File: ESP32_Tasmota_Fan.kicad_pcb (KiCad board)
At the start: 2 copper layers, 70 x 45 mm, 19 parts, among them J1 Conn_01x04, J2 Conn_01x06, J6 Conn_01x02_Female, J8 Conn_01x06, U1 mini_esp32

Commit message: Production Version
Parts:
- H1, H2, H3, H4: footprint MountingHole:MountingHole_3.2mm_M3_ISO7380 -> MountingHole:MountingHole_3.2mm_M3_Pad_Via
- moved J6 1.42 mm to (144.8, 133.5)
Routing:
- net Net-(D1-Pad2): track 0.00 -> 2.90 mm
- net +12V: track 99.6 -> 101.1 mm

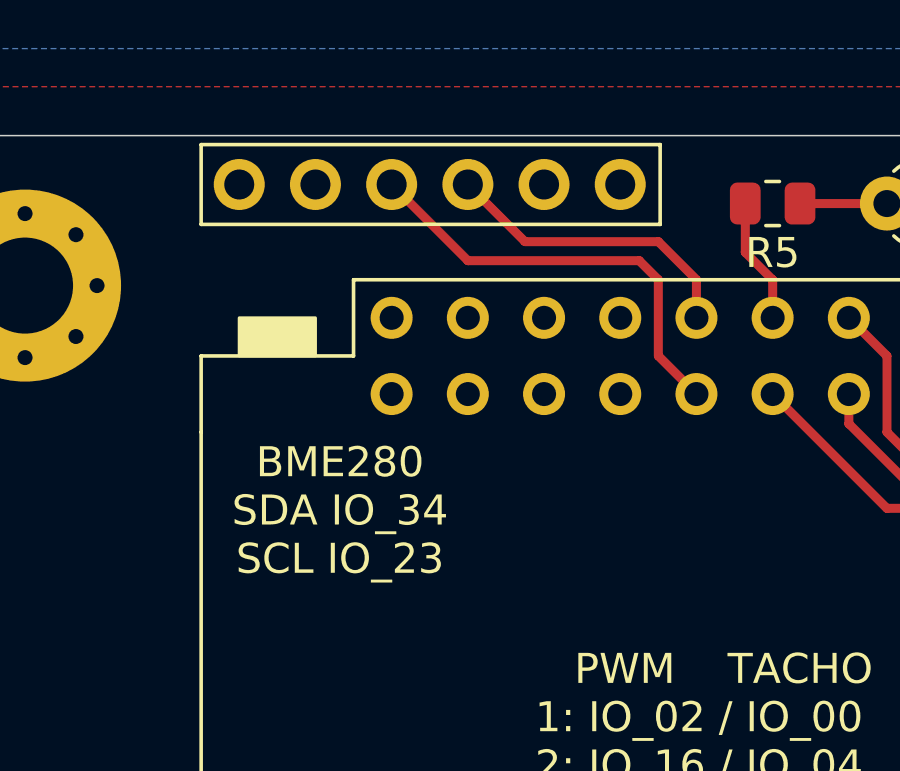
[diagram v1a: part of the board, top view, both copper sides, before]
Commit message: Move I2C Pins for BME280
IO34 can only do input, so it is not suitable for I2C
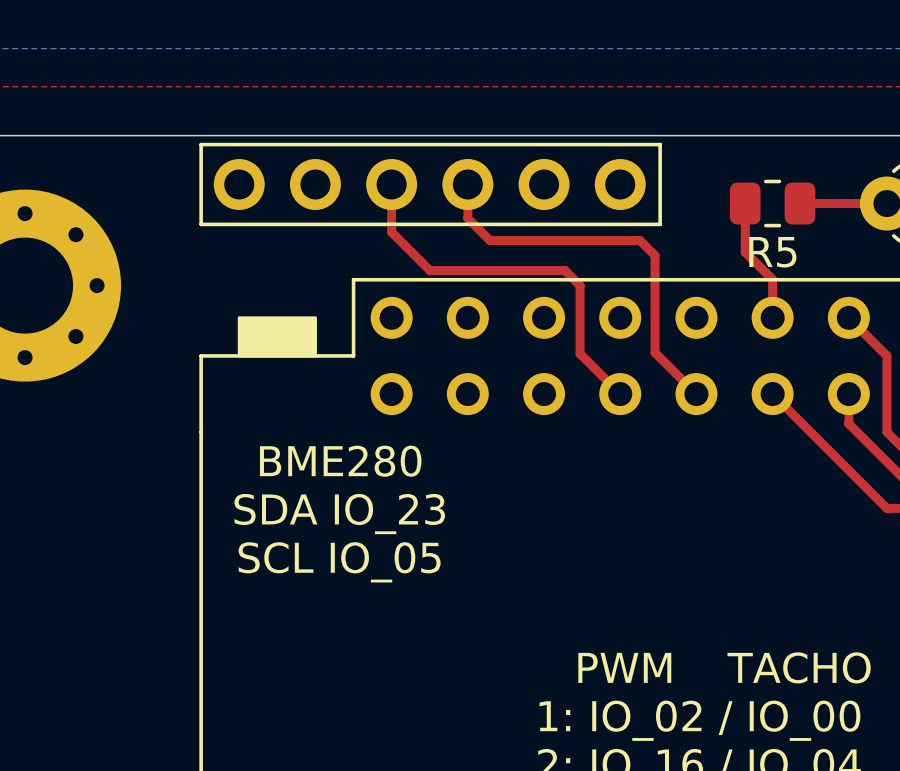
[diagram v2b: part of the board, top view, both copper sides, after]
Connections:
- U1 pad 11: SDA -> Net-(U1-Pad11)
- U1 pad 12: SCL -> SDA
- U1 pad 14: Net-(U1-Pad14) -> SCL
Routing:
- net SDA: track 10.2 -> 13.1 mm
- net SCL: track 14.5 -> 12.8 mm
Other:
- board text added: "BME280 SDA IO_23 SCL IO_05"
- board text removed: "BME280 SDA IO_34 SCL IO_23"

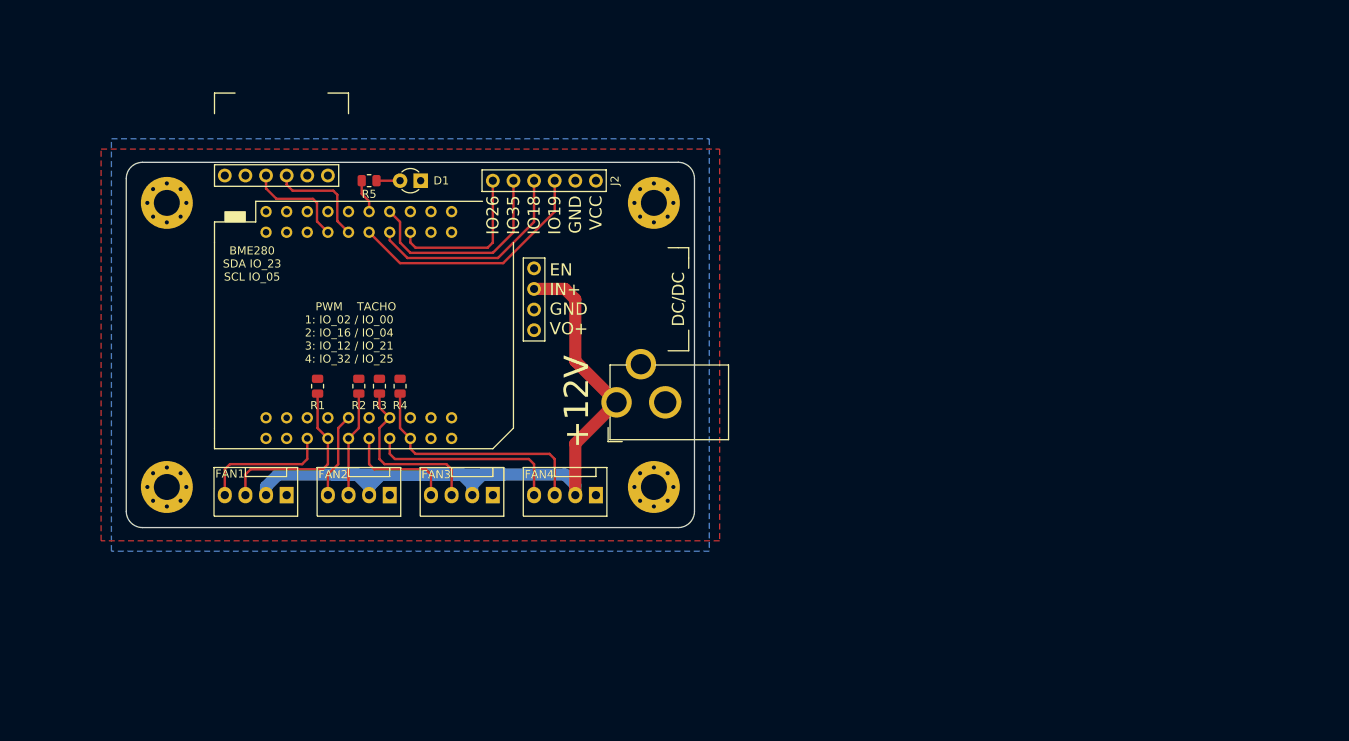
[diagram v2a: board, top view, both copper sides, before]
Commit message: First step for new design
split up design into multiples
added voltage regulator available at JLCPCB
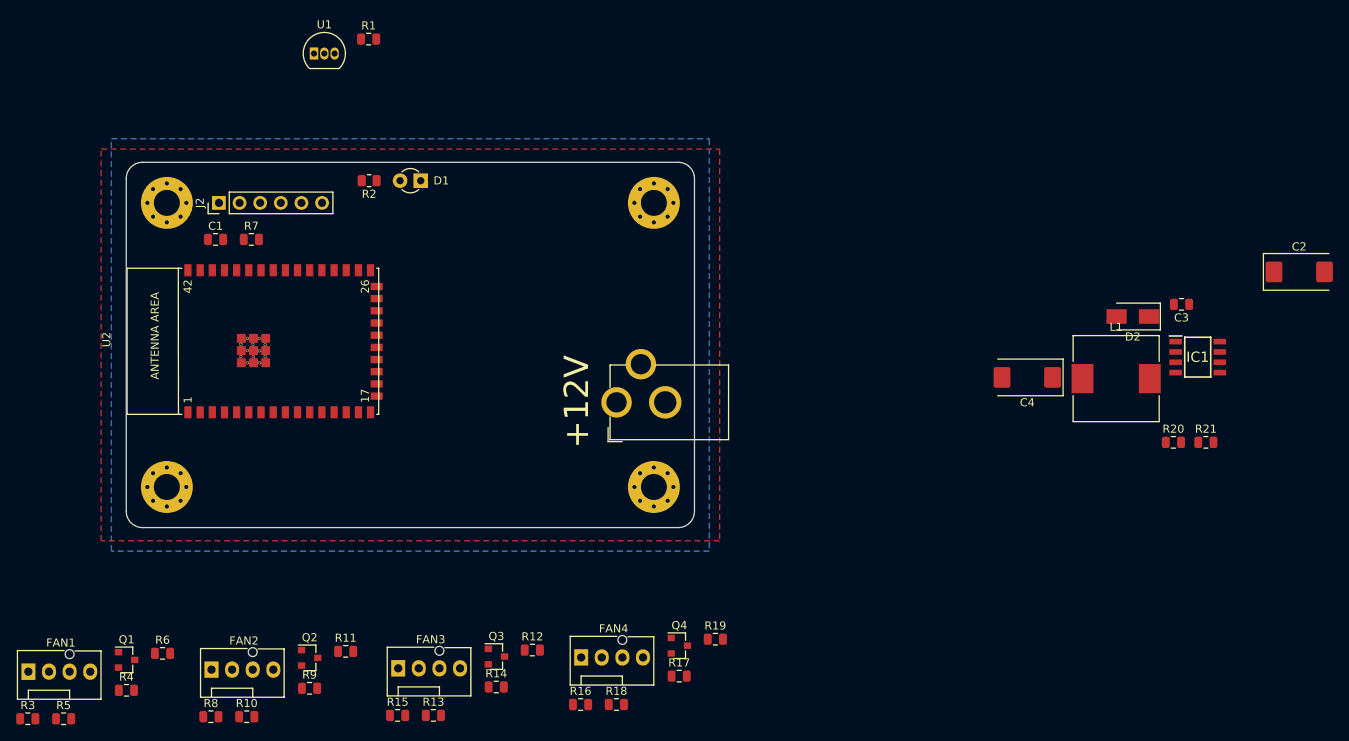
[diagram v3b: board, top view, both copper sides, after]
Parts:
- removed the J1 at (134.6, 117.0)
- removed J8: Conn_01x06, Connector_PinHeader_2.54mm:PinHeader_1x06_P2.54mm_Vertical
- removed the R2 at (113.0, 131.5)
- added C1: C_Small, Capacitor_SMD:C_0805_2012Metric, F.Cu at (95.4, 113.4)
- added C2: CP, Capacitor_Tantalum_SMD:CP_EIA-7343-30_AVX-N, F.Cu at (228.9, 117.4)
- added C3: C_Small, Capacitor_SMD:C_0805_2012Metric, F.Cu at (214.4, 121.4)
- added C4: CP, Capacitor_Tantalum_SMD:CP_EIA-7343-30_AVX-N, F.Cu at (195.4, 130.4)
- added D2: 1N5820/SS34, Diode_SMD:D_SMA, F.Cu at (208.4, 122.9)
- added IC1: XL1509-ADJE1, CSE:SOIC127P600X175-8N, F.Cu at (216.4, 127.9)
- added L1: INDUCTOR, Inductor_SMD:L_10.4x10.4_H4.8, F.Cu at (206.3, 130.6)
- added Q1: Q_PMOS_GDS, Package_TO_SOT_SMD:SOT-23, F.Cu at (84.4, 165.2)
- added Q2: Q_PMOS_GDS, Package_TO_SOT_SMD:SOT-23, F.Cu at (107.0, 165.0)
- added Q3: Q_PMOS_GDS, Package_TO_SOT_SMD:SOT-23, F.Cu at (130.0, 164.8)
- added Q4: Q_PMOS_GDS, Package_TO_SOT_SMD:SOT-23, F.Cu at (152.5, 163.5)
- added R10: 10k, Resistor_SMD:R_0805_2012Metric, F.Cu at (99.2, 172.2)
- added R11: 10k, Resistor_SMD:R_0805_2012Metric, F.Cu at (111.4, 164.2)
- added R12: 10k, Resistor_SMD:R_0805_2012Metric, F.Cu at (134.4, 164.0)
- added R13: 10k, Resistor_SMD:R_0805_2012Metric, F.Cu at (122.2, 172.1)
- added R14: 10k, Resistor_SMD:R_0805_2012Metric, F.Cu at (130.0, 168.6)
- added R15: 10k, Resistor_SMD:R_0805_2012Metric, F.Cu at (117.8, 172.1)
- added R16: 10k, Resistor_SMD:R_0805_2012Metric, F.Cu at (140.3, 170.7)
- added R17: 10k, Resistor_SMD:R_0805_2012Metric, F.Cu at (152.5, 167.2)
- added R18: 10k, Resistor_SMD:R_0805_2012Metric, F.Cu at (144.8, 170.7)
- added R19: 10k, Resistor_SMD:R_0805_2012Metric, F.Cu at (156.9, 162.7)
- added R20: 2k7, Resistor_SMD:R_0805_2012Metric, F.Cu at (213.4, 138.4)
- added R21: 1k6, Resistor_SMD:R_0805_2012Metric, F.Cu at (217.4, 138.4)
- added R5: 10k, Resistor_SMD:R_0805_2012Metric, F.Cu at (76.7, 172.5)
- added R6: 10k, Resistor_SMD:R_0805_2012Metric, F.Cu at (88.8, 164.4)
- added R7: R_Small, Resistor_SMD:R_0805_2012Metric, F.Cu at (99.8, 113.4)
- added R8: 10k, Resistor_SMD:R_0805_2012Metric, F.Cu at (94.8, 172.2)
- added R9: 10k, Resistor_SMD:R_0805_2012Metric, F.Cu at (107.0, 168.7)
- added U2: esp32-s2-wroom, ESP32-S2:esp32-s2-wrooom, F.Cu at (99.9, 125.9)
- R1: value 10k -> 4k7
- U1: value mini_esp32 -> DS18B20; footprint ESP32_mini:ESP32_mini -> Package_TO_SOT_THT:TO-92_Inline
- moved R3 59.6 mm to (72.2, 172.5), turned to 0 degrees
- moved R4 50.4 mm to (84.4, 169.0), turned to 0 degrees
- moved J2 46.5 mm to (95.8, 108.9), turned to 90 degrees
- moved R1 43.2 mm to (114.2, 88.7), turned to 0 degrees
- moved FAN1 38.5 mm to (72.3, 166.7), turned to 0 degrees
- moved U1 33.9 mm to (107.5, 90.5), turned to 0 degrees
- moved FAN2 30.7 mm to (94.9, 166.4), turned to 0 degrees
- moved FAN3 24.3 mm to (117.9, 166.3), turned to 0 degrees
- moved FAN4 20.1 mm to (140.4, 164.9), turned to 0 degrees
- renumbered J6 to J1, R5 to R2
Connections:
- FAN1 pad 2: +12V -> /FAN 1/SPLY
- FAN1 pad 3: SENSE1 -> /FAN 1/SENSE
- FAN1 pad 4: PWM1 -> /FAN 1/PWM_Ctrl
- FAN2 pad 2: +12V -> /sheet6191C4D9/SPLY
- FAN2 pad 3: SENSE2 -> /sheet6191C4D9/SENSE
- FAN2 pad 4: PWM2 -> /sheet6191C4D9/PWM_Ctrl
- FAN3 pad 2: +12V -> /sheet6191C6A1/SPLY
- FAN3 pad 3: SENSE3 -> /sheet6191C6A1/SENSE
- FAN3 pad 4: PWM3 -> /sheet6191C6A1/PWM_Ctrl
- FAN4 pad 2: +12V -> /sheet6191C855/SPLY
- FAN4 pad 3: SENSE4 -> /sheet6191C855/SENSE
- FAN4 pad 4: PWM4 -> /sheet6191C855/PWM_Ctrl
- J2 pad 1: +3V3 -> GND
- J2 pad 2: GND -> /ESP32 Core/EN
- J2 pad 3: IO19 -> /ESP32 Core/IO0
- J2 pad 4: IO18 -> /ESP32 Core/RX
- J2 pad 5: IO35 -> /ESP32 Core/TX
- J2 pad 6: IO26 -> +3V3
- R1 pad 2: SENSE1 -> Net-(R1-Pad2)
- R3 pad 1: +3V3 -> /FAN 1/SW
- R3 pad 2: SENSE3 -> Net-(Q1-Pad1)
- R4 pad 1: +3V3 -> /FAN 1/PWM
- R4 pad 2: SENSE4 -> /FAN 1/PWM_Ctrl
- U1 pad 2: Net-(U1-Pad2) -> Net-(R1-Pad2)
- U1 pad 3: Net-(U1-Pad3) -> +3V3
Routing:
- net +12V: track 101.1 -> 0.00 mm
- net IO19: track 30.9 -> 0.00 mm
- net SENSE4: track 30.1 -> 0.00 mm
- net IO18: track 26.6 -> 0.00 mm
- net IO35: track 26.2 -> 0.00 mm
- net PWM4: track 24.0 -> 0.00 mm
- net SENSE1: track 22.4 -> 0.00 mm
- net SENSE3: track 21.7 -> 0.00 mm
- net IO26: track 19.6 -> 0.00 mm
- net PWM1: track 16.4 -> 0.00 mm
- net PWM3: track 13.9 -> 0.00 mm
- net SDA: track 13.1 -> 0.00 mm
- net SENSE2: track 13.0 -> 0.00 mm
- net SCL: track 12.8 -> 0.00 mm
- net PWM2: track 10.6 -> 0.00 mm
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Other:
- board text removed: "BME280 SDA IO_23 SCL IO_05"
- board text removed: "DC/DC"
- board text removed: "EN IN+ GND VO+"
- board text removed: "ESP32 PWMFan Controller"
- board text removed: "GND"
- board text removed: "IO18"
- board text removed: "IO19"
- board text removed: "IO26"
- board text removed: "IO35"
- board text removed: "PWM TACHO 1: IO_02 / IO_00 2: IO_16 / IO_04 3: IO_12 / IO_21 4: IO_32 / IO_25"
- board text removed: "VCC"
- board text removed: "zeroflow"

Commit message: First layouting
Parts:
- moved C2 140.0 mm to (88.9, 119.5), turned to 90 degrees
- moved C3 120.0 mm to (94.6, 113.8), turned to 90 degrees
- moved R21 119.4 mm to (99.5, 119.6), turned to 180 degrees
- moved IC1 118.0 mm to (99.2, 113.8), turned to 90 degrees
- moved R20 112.0 mm to (103.0, 119.6), turned to 180 degrees
- moved D2 110.9 mm to (98.6, 107.5)
- moved L1 99.5 mm to (108.6, 111.9)
- moved C4 75.3 mm to (121.3, 117.0), turned to 90 degrees
- moved U1 64.9 mm to (151.8, 137.9), turned to 90 degrees
- moved R1 59.5 mm to (145.7, 139.2)
- moved J2 56.7 mm to (151.9, 117.2), turned to 0 degrees
- moved R3 53.5 mm to (103.5, 129.1), turned to 180 degrees
- moved R5 53.2 mm to (103.5, 126.5)
- moved C1 52.2 mm to (147.3, 118.3)
- moved J1 50.2 mm to (94.6, 131.6), turned to 270 degrees
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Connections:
- net /ESP32 Core/IO1 renamed /SENSE1
- net /ESP32 Core/IO2 renamed /SENSE2
- net /ESP32 Core/IO3 renamed /SENSE3
- net /ESP32 Core/IO4 renamed /SENSE4
- D2 pad 1: Net-(D2-Pad1) -> /DC/DC Buck/OUTPUT
- IC1 pad 2: Net-(D2-Pad1) -> /DC/DC Buck/OUTPUT
- L1 pad 1: +3V3 -> /DC/DC Buck/OUTPUT
- L1 pad 2: Net-(D2-Pad1) -> +3V3
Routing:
- net +12V: track 0.00 -> 37.0 mm
- net /sheet6191C855/SPLY: track 0.00 -> 28.7 mm
- net /sheet6191C6A1/SPLY: track 0.00 -> 21.3 mm
- net /DC/DC Buck/OUTPUT: track 0.00 -> 16.5 mm
- net +3V3: track 0.00 -> 13.7 mm
- net /sheet6191C4D9/SPLY: track 0.00 -> 13.3 mm
- net GND: track 0.00 -> 7.74 mm
- net /FAN 1/SPLY: track 0.00 -> 7.26 mm
- net /DC/DC Buck/FB: track 0.00 -> 4.87 mm
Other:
- board text removed: "+12V"
